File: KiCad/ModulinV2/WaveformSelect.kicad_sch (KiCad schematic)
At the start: 3 parts, among them IC8 SN74HC193DR

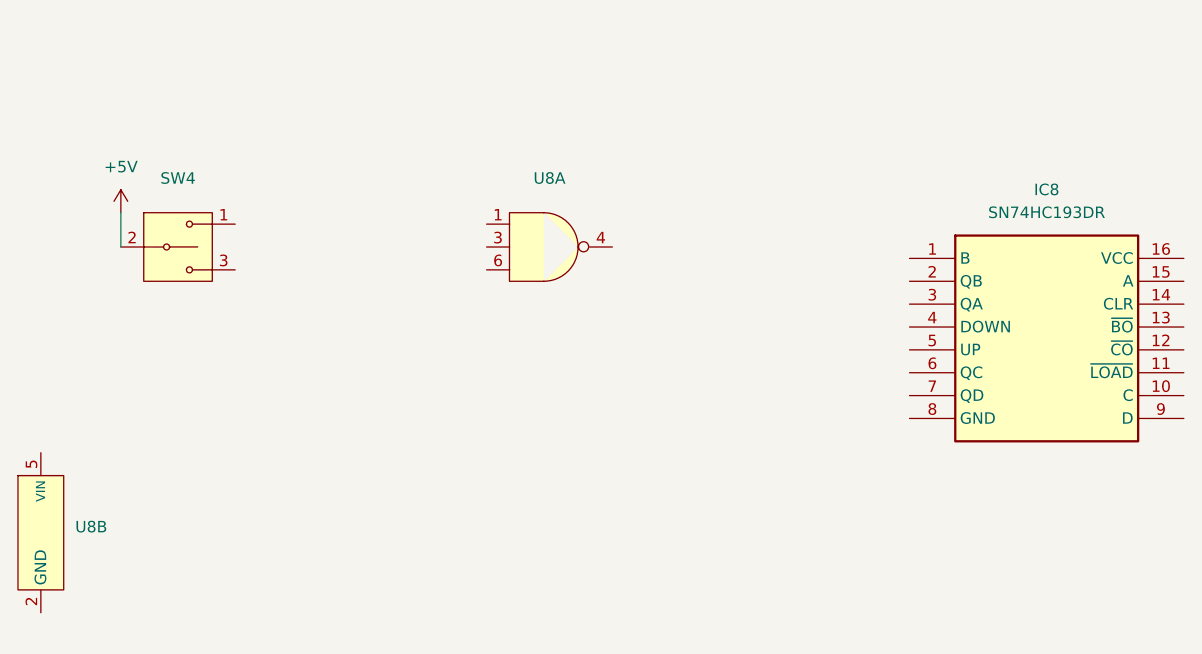
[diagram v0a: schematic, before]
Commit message: Modified Octave selector and started on waveform selection
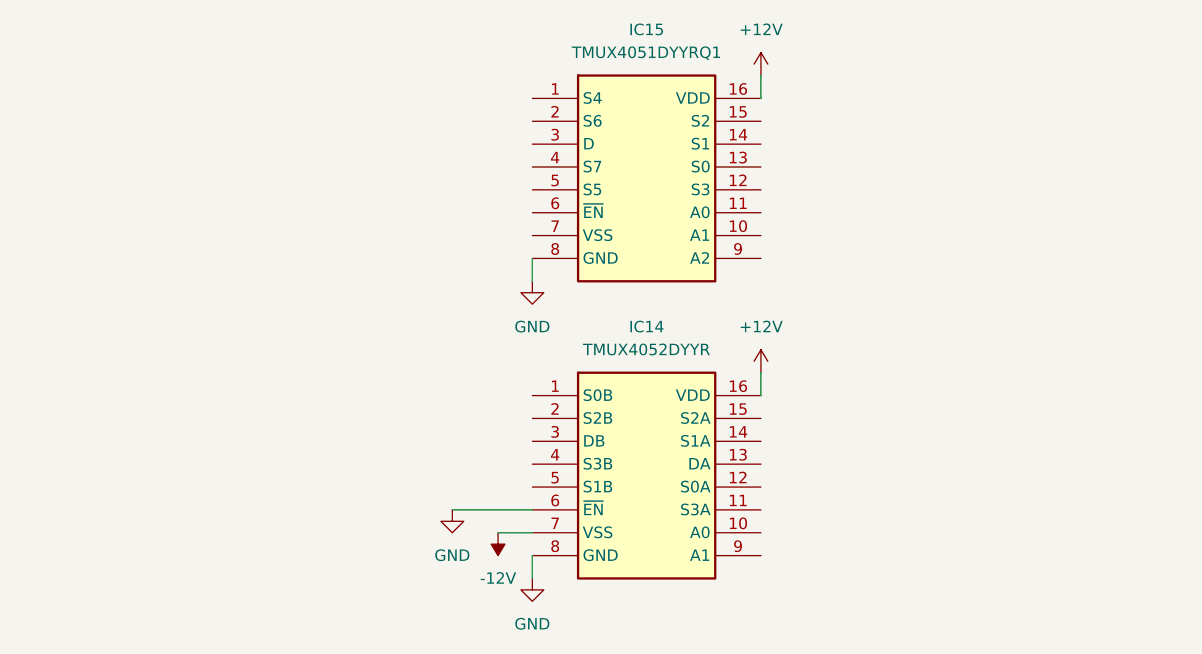
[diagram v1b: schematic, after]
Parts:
- removed IC8: SN74HC193DR, SOIC127P600X175-16N, symbol SN74HC193DR:SN74HC193DR
- removed SW4: ~, symbol RB14DE1100:RB14DE1100
- removed U8: ~, symbol SN74LVC1G10DCKR:SN74LVC1G10DCKR_Alt
- added IC14: TMUX4052DYYR, SOP50P326X110-16N, symbol TMUX4052DYYR:TMUX4052DYYR
- added IC15: TMUX4051DYYRQ1, SOP50P326X110-16N, symbol TMUX4051DYYRQ1:TMUX4051DYYRQ1
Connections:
- new net +12V: IC14.16 (VDD), IC15.16 (VDD)
- new net -12V: IC14.7 (VSS)
- new net GND: IC14.6 (~{EN}), IC14.8 (GND), IC15.8 (GND)
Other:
- title: Waveform Selector -> Octave Selector

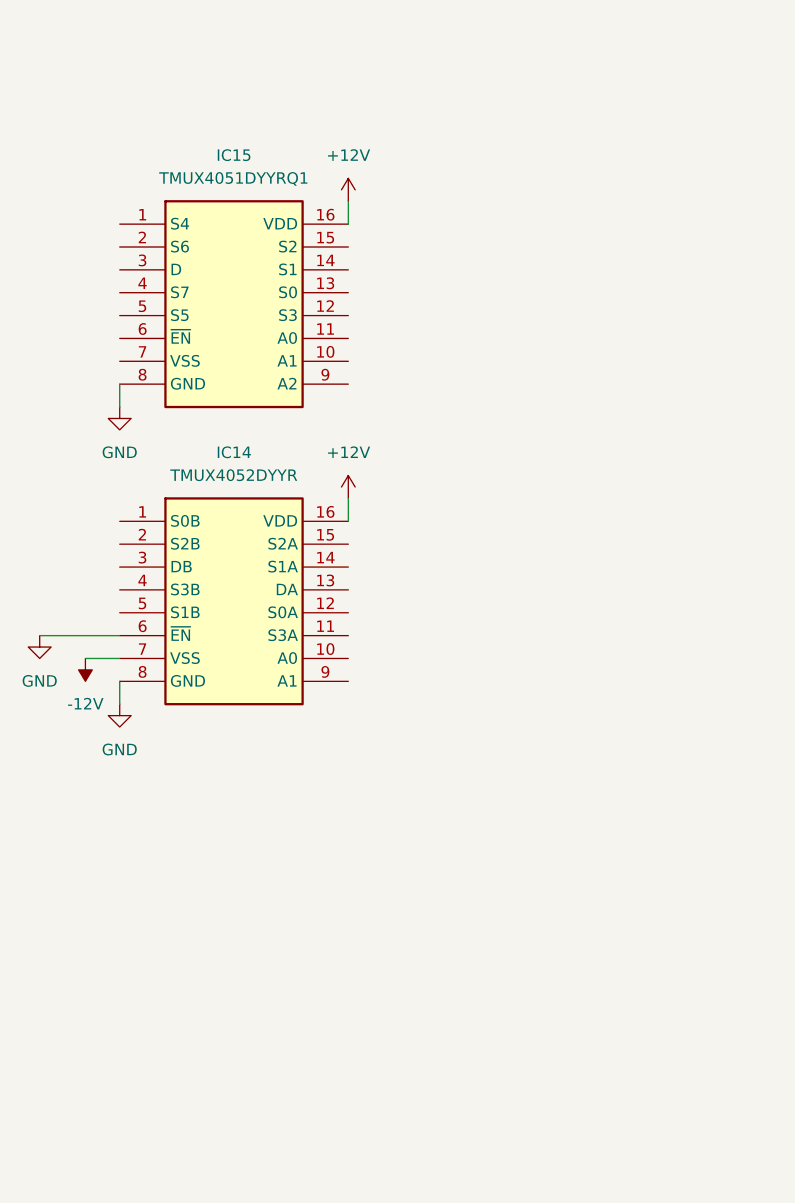
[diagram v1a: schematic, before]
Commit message: Modified USB connection and added LEDs
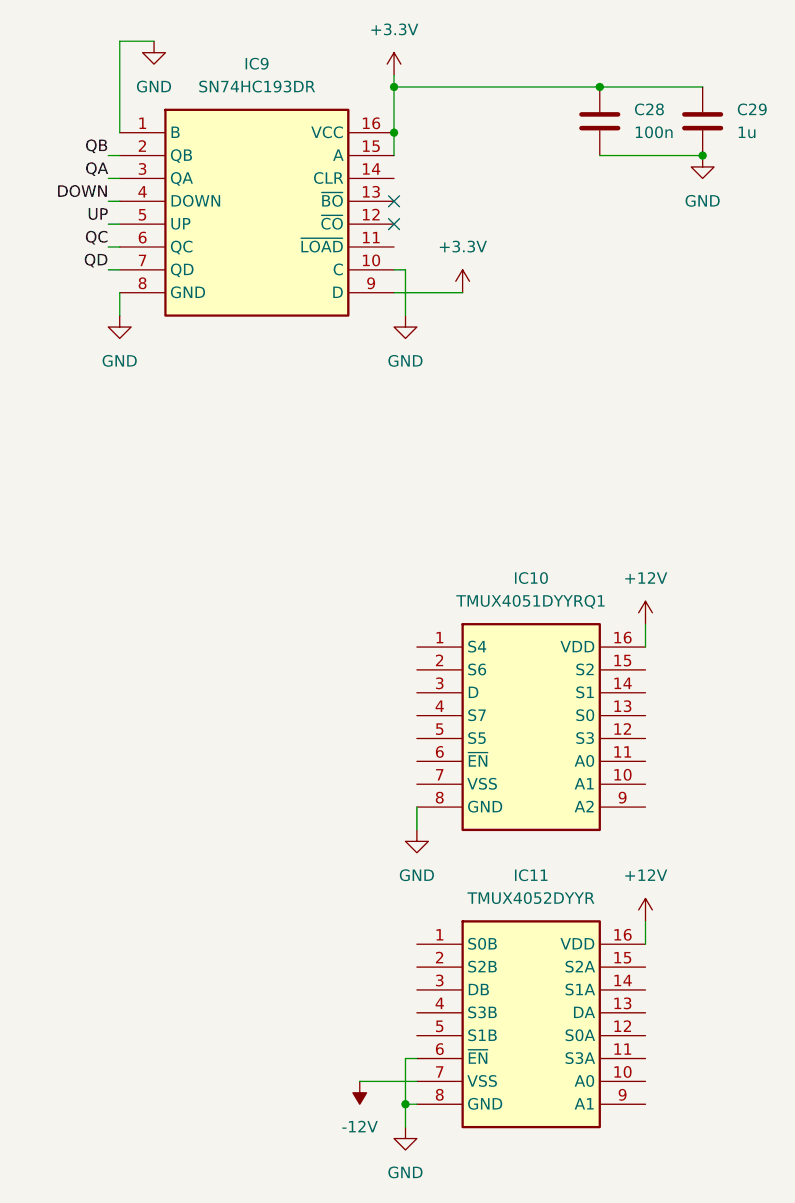
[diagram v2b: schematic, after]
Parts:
- added C28: 100n, symbol Device:C
- added C29: 1u, symbol Device:C
- added IC9: SN74HC193DR, SOIC127P600X175-16N, symbol SN74HC193DR:SN74HC193DR
- renumbered IC15 to IC10, IC14 to IC11
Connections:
- net GND: now also C28.1, C29.1, IC9.1 (B), IC9.10 (C), IC9.8 (GND)
- new net +3.3V: C28.2, C29.2, IC9.15 (A), IC9.16 (VCC), IC9.9 (D)
- new net DOWN: IC9.4 (DOWN)
- new net QA: IC9.3 (QA)
- new net QB: IC9.2 (QB)
- new net QC: IC9.6 (QC)
- new net QD: IC9.7 (QD)
- new net UP: IC9.5 (UP)
- no-connect marks 0 -> 2
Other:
- moved on the sheet: IC10, IC11

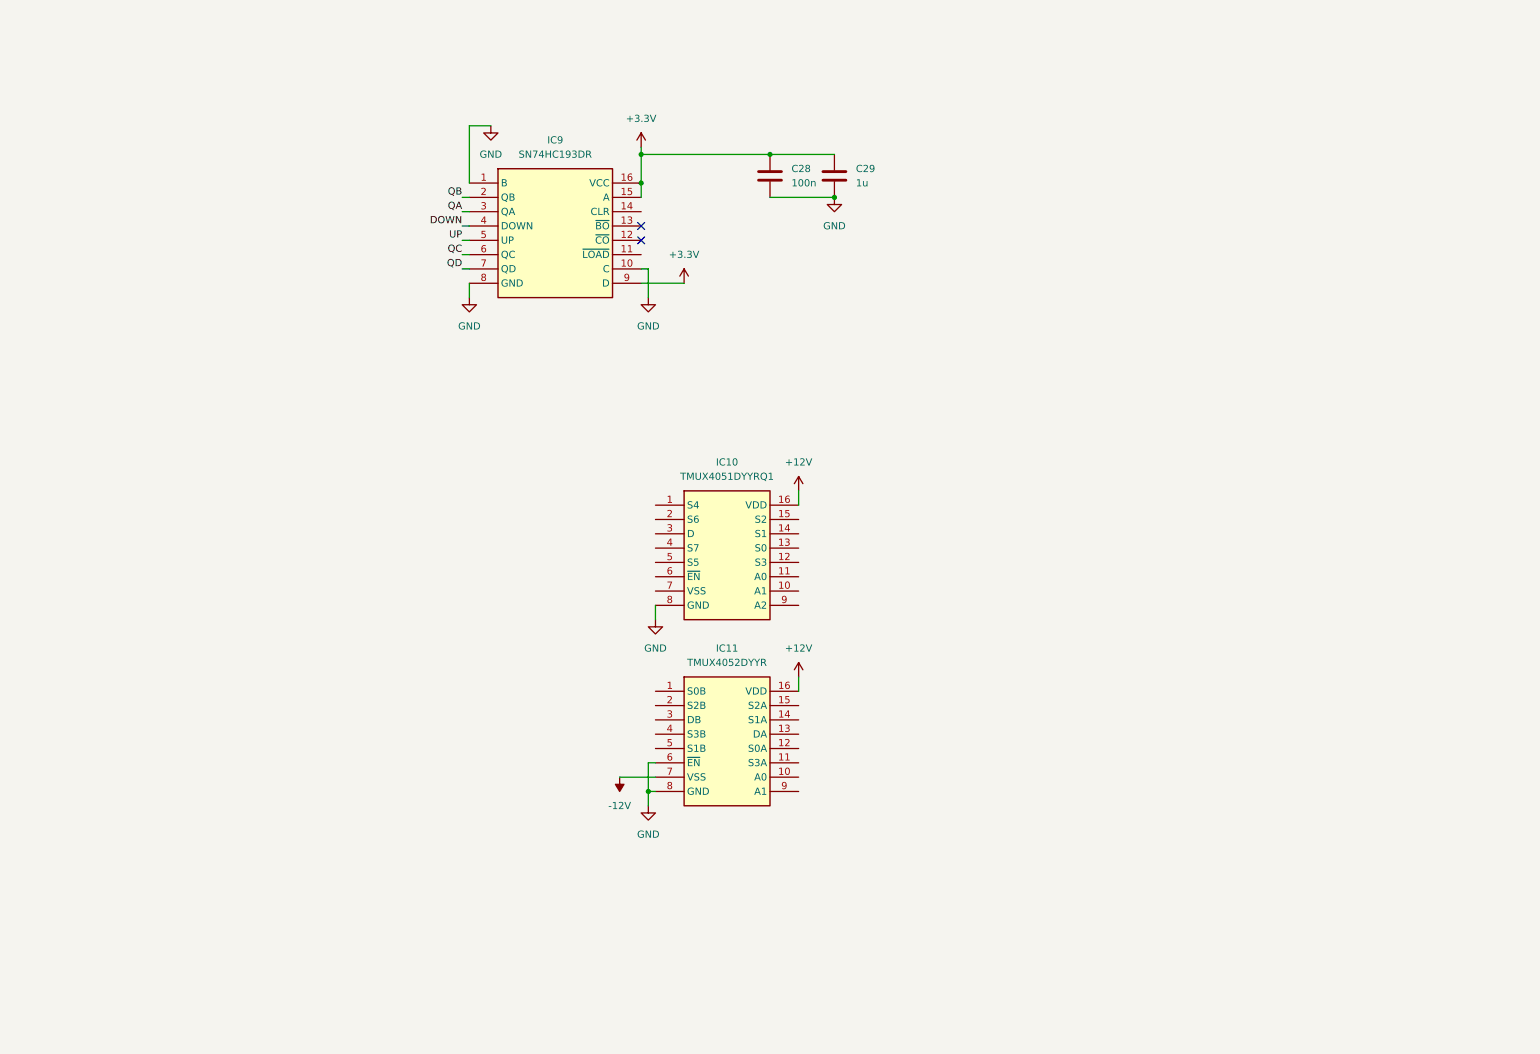
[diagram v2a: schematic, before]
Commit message: Fleshed out the waveform select schematic a bit + general cleanup
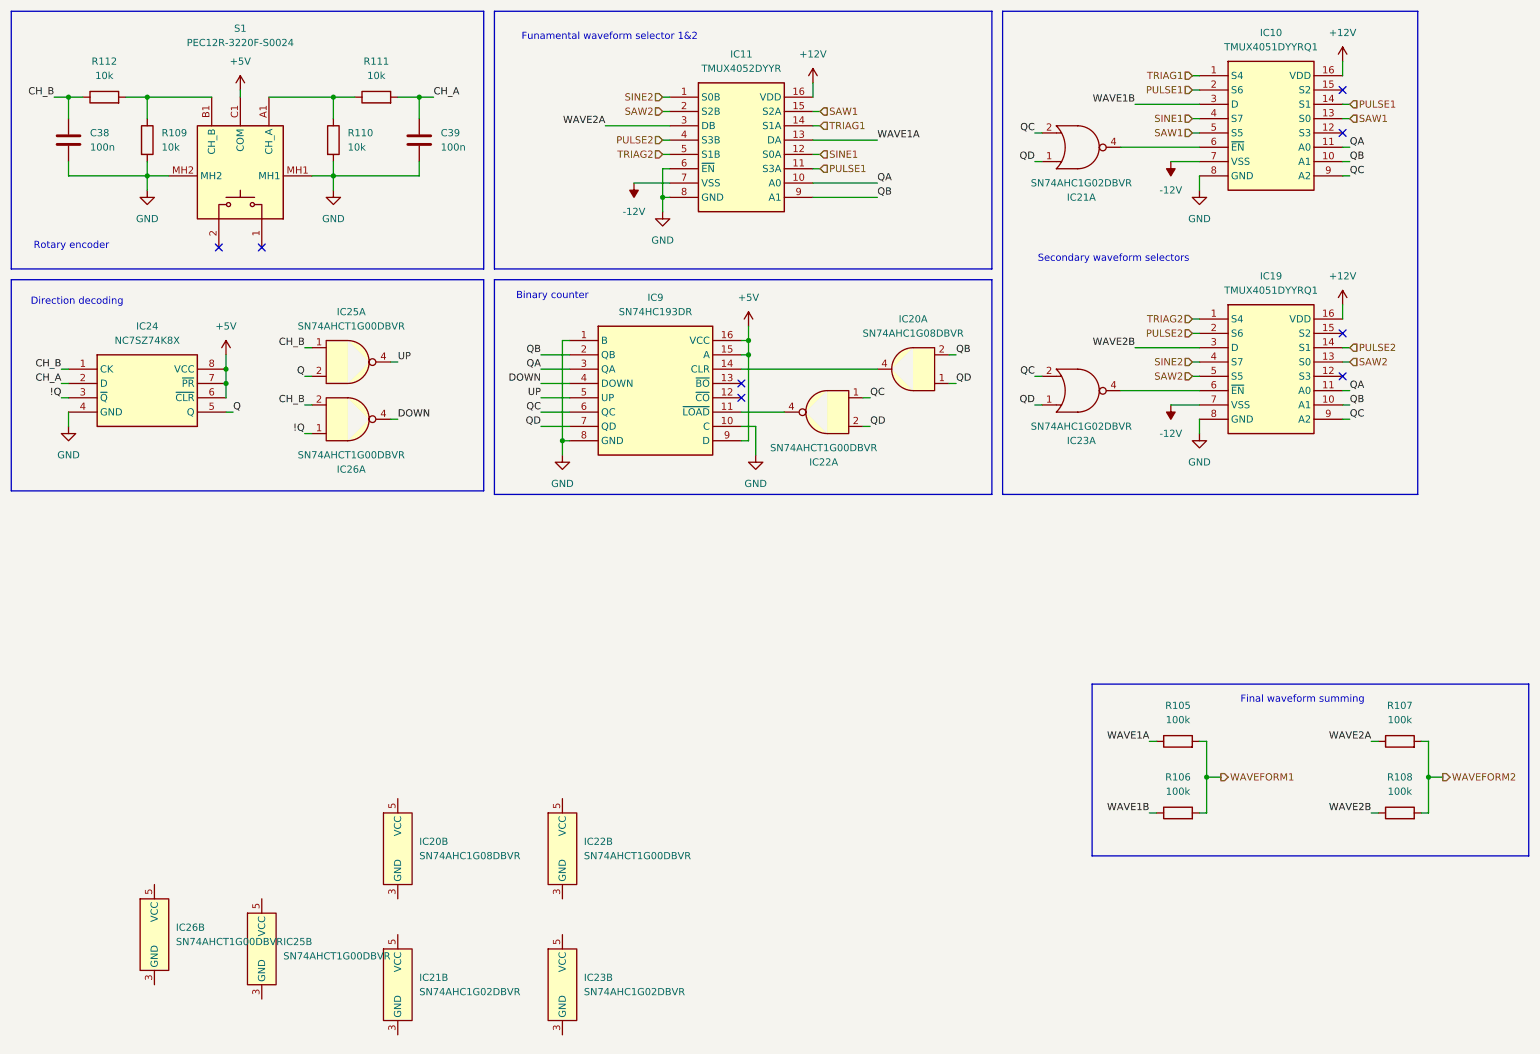
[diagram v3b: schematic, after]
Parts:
- removed C28: 100n, symbol Device:C
- removed C29: 1u, symbol Device:C
- added C38, C39: 100n, symbol Device:C
- added IC19: TMUX4051DYYRQ1, SOP50P326X110-16N, symbol TMUX4051DYYRQ1:TMUX4051DYYRQ1
- added IC20: SN74AHC1G08DBVR, symbol SN74AHC1G08DBVR:SN74AHC1G08DBVR_Alt
- added IC21, IC23: SN74AHC1G02DBVR, symbol SN74AHC1G02DBVR:SN74AHC1G02DBVR_Alt
- added IC22, IC25, IC26: SN74AHCT1G00DBVR, symbol SN74AHCT1G00DBVR:SN74AHCT1G00DBVR_Alt
- added IC24: NC7SZ74K8X, SOP50P310X90-8N, symbol NC7SZ74K8X:NC7SZ74K8X
- added R105, R106, R107, R108: 100k, symbol Device:R
- added R109, R110, R111, R112: 10k, symbol Device:R
- added S1: PEC12R-3220F-S0024, PEC12R3220FS0024, symbol PEC12R-3220F-S0024:PEC12R-3220F-S0024
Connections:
- net +12V: now also IC19.16 (VDD)
- net -12V: now also IC10.7 (VSS), IC19.7 (VSS)
- net DOWN: now also IC26.4
- net GND: now also C38.2, C39.2, IC19.8 (GND), IC24.4 (GND), R109.2, R110.2, S1.MH1, S1.MH2
- net QA: now also IC10.11 (A0), IC11.10 (A0), IC19.11 (A0)
- net QB: now also IC10.10 (A1), IC11.9 (A1), IC19.10 (A1), IC20.2
- net QC: now also IC10.9 (A2), IC19.9 (A2), IC21.2, IC22.1, IC23.2
- net QD: now also IC20.1, IC21.1, IC22.2, IC23.1
- net UP: now also IC25.4
- net at IC9.11 (~{LOAD}): now also IC22.4
- net at IC9.14 (CLR): now also IC20.4
- net SINE2: now reaches IC11.1 (S0B)
- net SINE2: now also IC19.4 (S7)
- net PULSE1: now reaches IC11.11 (S3A)
- net PULSE1: now also IC10.14 (S1), IC10.2 (S6)
- net SINE1: now reaches IC11.12 (S0A)
- net SINE1: now also IC10.4 (S7)
- net WAVE1A: now reaches IC11.13 (DA)
- net WAVE1A: now also R105.1
- net TRIAG1: now reaches IC11.14 (S1A)
- net TRIAG1: now also IC10.1 (S4)
- net SAW1: now reaches IC11.15 (S2A)
- net SAW1: now also IC10.13 (S0), IC10.5 (S5)
- net SAW2: now reaches IC11.2 (S2B)
- net SAW2: now also IC19.13 (S0), IC19.5 (S5)
- net WAVE2A: now reaches IC11.3 (DB)
- net WAVE2A: now also R107.1
- net PULSE2: now reaches IC11.4 (S3B)
- net PULSE2: now also IC19.14 (S1), IC19.2 (S6)
- net TRIAG2: now reaches IC11.5 (S1B)
- net TRIAG2: now also IC19.1 (S4)
- net WAVE1B: now reaches IC10.3 (D)
- net WAVE1B: now also R106.1
- net at IC10.6 (~{EN}): now also IC21.4
- net +3.3V renamed +5V
- net +5V: now also IC24.6 (~{CLR}), IC24.7 (~{PR}), IC24.8 (VCC), S1.C1 (COM)
- new net: IC19.6 (~{EN}), IC23.4
- new net: R109.1, R112.2, S1.B1 (CH_B)
- new net: R110.1, R111.1, S1.A1 (CH_A)
- new net !Q: IC24.3 (~{Q}), IC26.1
- new net CH_A: C39.1, IC24.2 (D), R111.2
- new net CH_B: C38.1, IC24.1 (CK), IC25.1, IC26.2, R112.1
- new net Q: IC24.5 (Q), IC25.2
- new net WAVE2B: IC19.3 (D), R108.1
- new net WAVEFORM1: R105.2, R106.2
- new net WAVEFORM2: R107.2, R108.2
- no-connect marks 2 -> 8
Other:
- note added: "Binary counter"
- note added: "Direction decoding"
- note added: "Final waveform summing"
- note added: "Funamental waveform selector 1&2"
- note added: "Rotary encoder"
- note added: "Secondary waveform selectors"
- moved on the sheet: IC10, IC11, IC9

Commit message: Added initial power supply schematic and modified MCU components
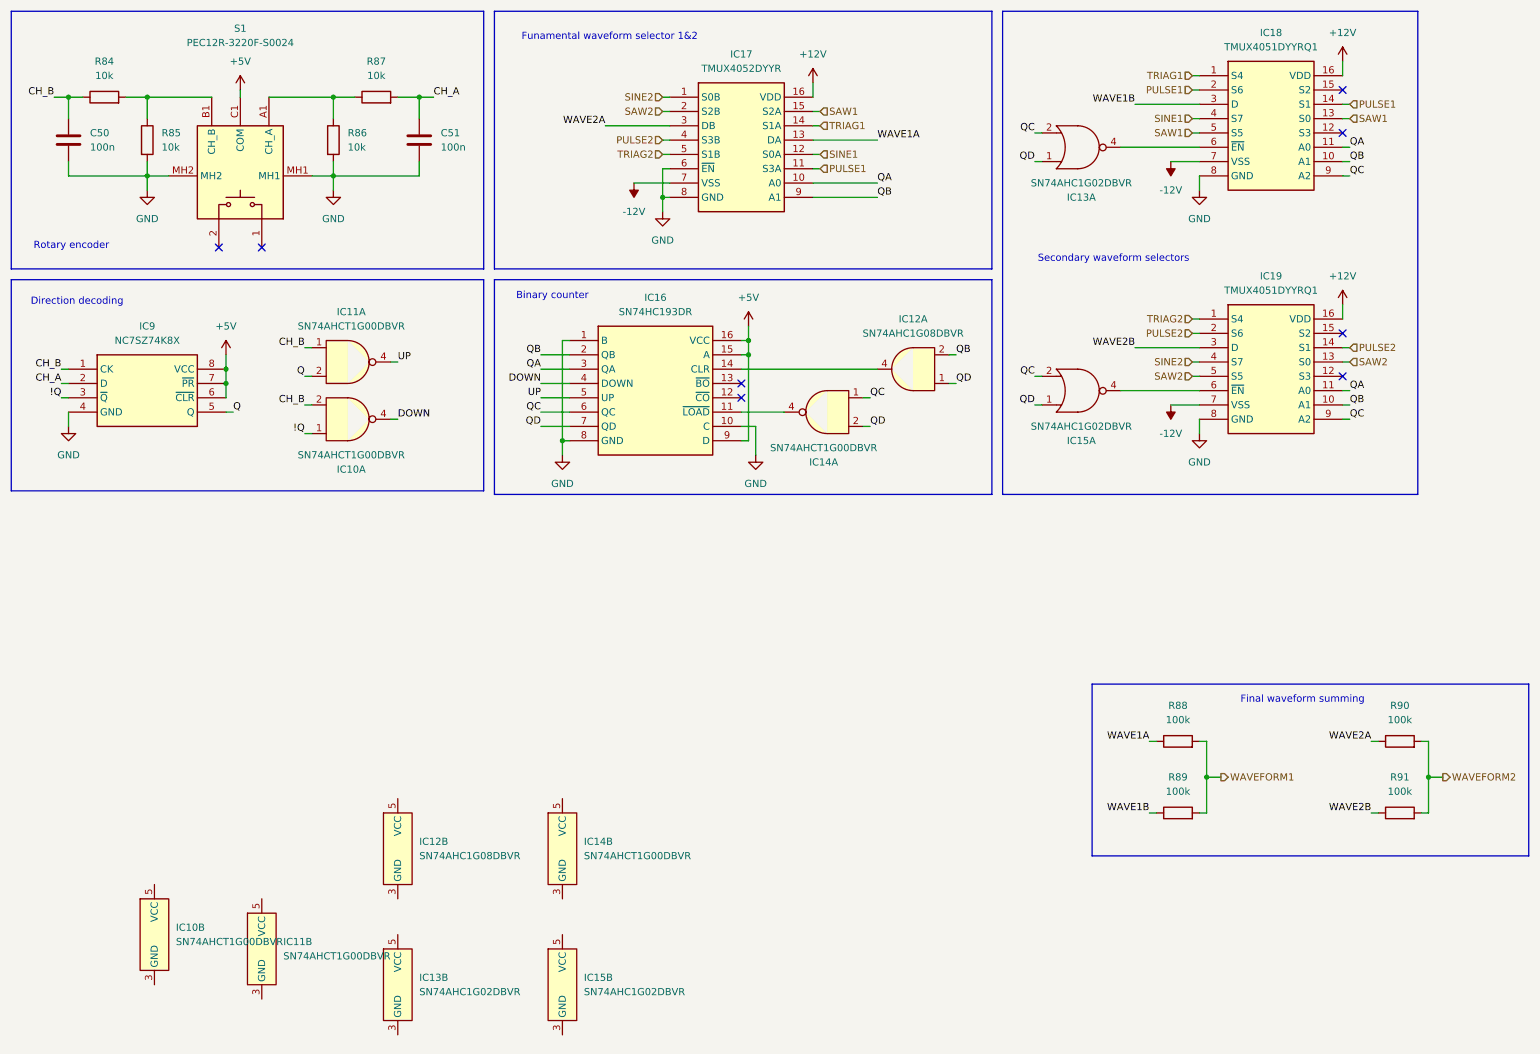
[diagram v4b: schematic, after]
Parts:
- renumbered C38 to C50, C39 to C51, IC26 to IC10, IC25 to IC11, IC20 to IC12, IC21 to IC13, IC22 to IC14, IC23 to IC15, IC9 to IC16, IC11 to IC17, IC10 to IC18, IC24 to IC9, R112 to R84, R109 to R85, R110 to R86, R111 to R87, R105 to R88, R106 to R89, R107 to R90, R108 to R91
